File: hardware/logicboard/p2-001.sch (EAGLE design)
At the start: 29 parts, among them IC1 5V, IC2 74LS07N, IC3 4066N, K1 G5V1, T1 2SC1815, U1 DS18B20

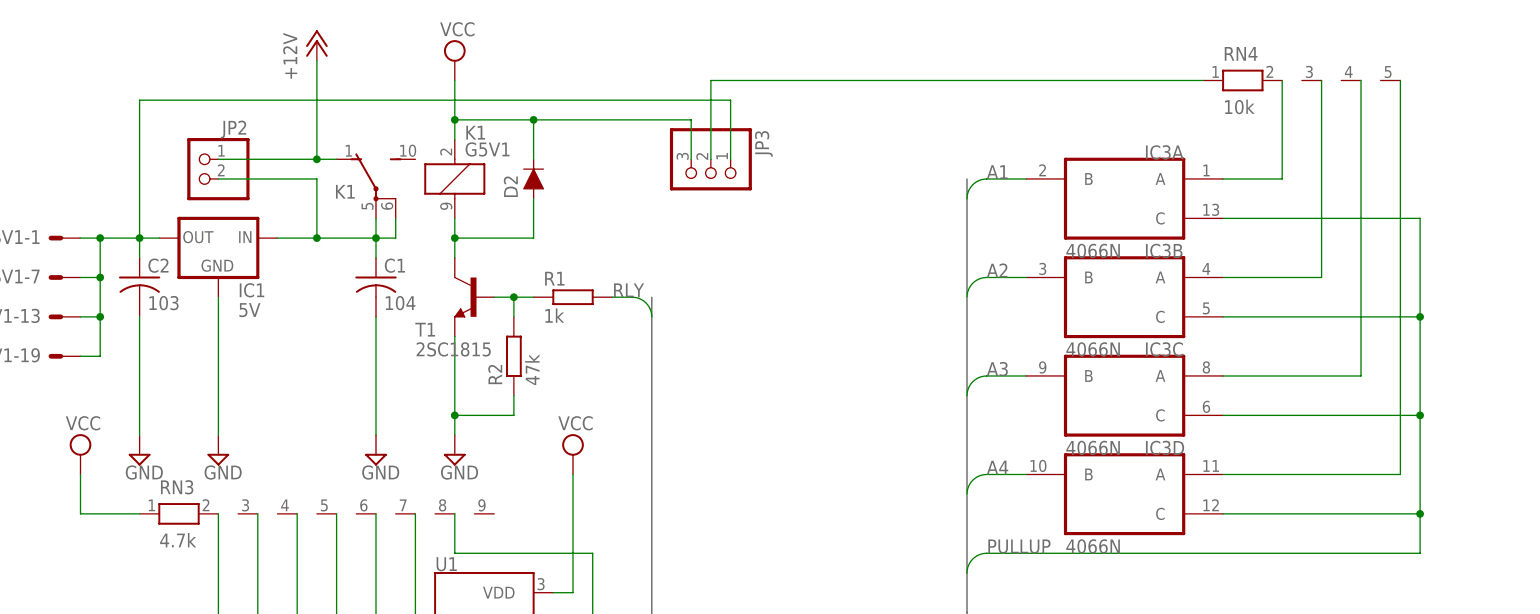
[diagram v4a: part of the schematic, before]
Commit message: Jumper -> SW.
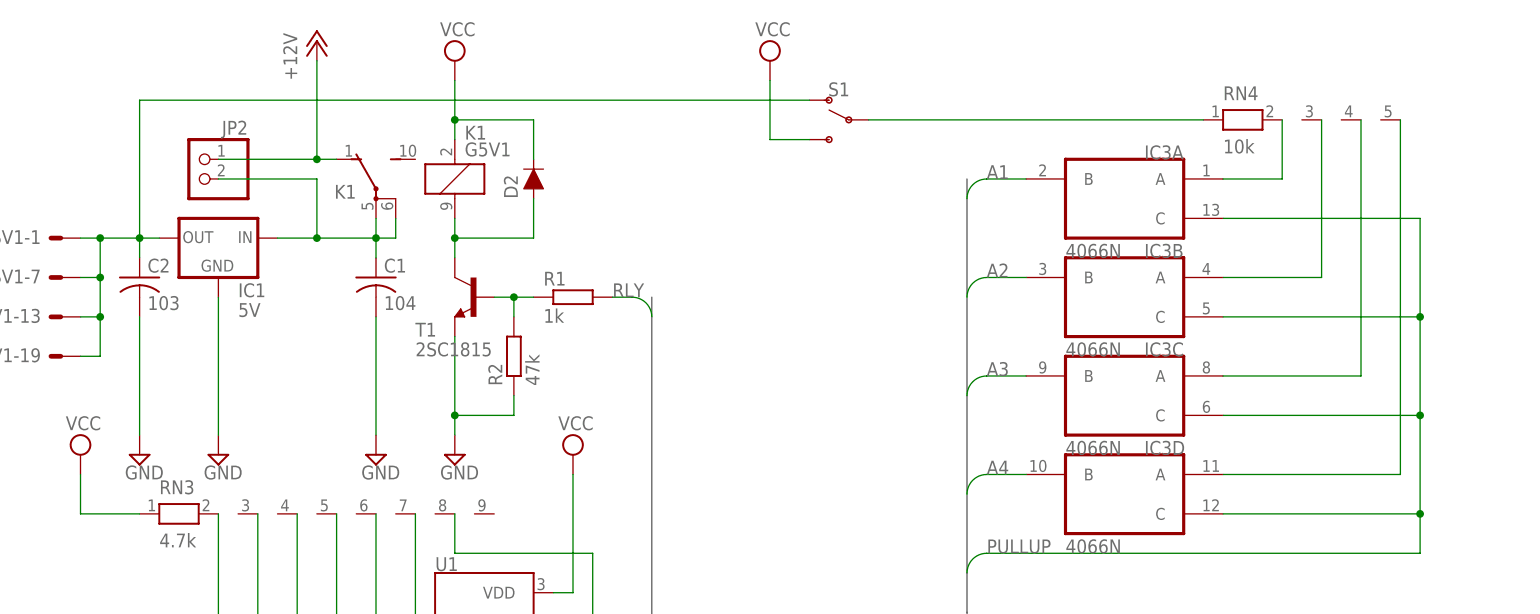
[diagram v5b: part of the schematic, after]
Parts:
- removed JP3: (no value), pinhead:PINHD-1X3
- added S1: (no value), SparkFun-Switches:SWITCH-SPDT-PTH-11.6X4.0MM
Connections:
- removed net N$2: JP3.2, RN4.1
- new net VPULLUP: RN4.1, S1.P
- net VCC: now also S1.S; no longer JP3.3
- net VOUT: now also S1.O; no longer JP3.1
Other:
- moved on the sheet: RN4
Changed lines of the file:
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@@
 <part name="SUPPLY28" library="supply2" deviceset="GND" device=""/>
 <part name="JP2" library="pinhead" library_urn="urn:adsk.eagle:library:325" deviceset="PINHD-1X2" device="" package3d_urn="urn:adsk.eagle:package:22435/2"/>
-<part name="JP3" library="pinhead" library_urn="urn:adsk.eagle:library:325" deviceset="PINHD-1X3" device="" package3d_urn="urn:adsk.eagle:package:22458/2"/>
+<part name="SUPPLY5" library="supply2" library_urn="urn:adsk.eagle:library:372" deviceset="VCC" device=""/>
+<part name="S1" library="SparkFun-Switches" deviceset="SWITCH-SPDT" device="-PTH-11.6X4.0MM"/>
 </parts>
 <sheets>
@@
 <attribute name="VALUE" x="122.555" y="6.985" size="1.778" layer="96"/>
 </instance>
-<instance part="RN4" gate="1" x="175.26" y="248.92" smashed="yes">
-<attribute name="NAME" x="172.72" y="251.46" size="1.778" layer="95"/>
-<attribute name="VALUE" x="172.72" y="244.602" size="1.778" layer="96"/>
+<instance part="RN4" gate="1" x="175.26" y="243.84" smashed="yes">
+<attribute name="NAME" x="172.72" y="246.38" size="1.778" layer="95"/>
+<attribute name="VALUE" x="172.72" y="239.522" size="1.778" layer="96"/>
 </instance>
 <instance part="IC3" gate="A" x="160.02" y="233.68" smashed="yes" rot="MR0">
@@
 <attribute name="VALUE" x="46.99" y="231.14" size="1.778" layer="96" rot="MR0"/>
 </instance>
-<instance part="JP3" gate="A" x="106.68" y="236.22" smashed="yes" rot="R270">
-<attribute name="NAME" x="112.395" y="242.57" size="1.778" layer="95" rot="R270"/>
-<attribute name="VALUE" x="99.06" y="242.57" size="1.778" layer="96" rot="R270"/>
+<instance part="SUPPLY5" gate="G$1" x="114.3" y="251.46" smashed="yes">
+<attribute name="VALUE" x="112.395" y="254.635" size="1.778" layer="96"/>
+</instance>
+<instance part="S1" gate="1" x="124.46" y="243.84" smashed="yes" rot="MR0">
+<attribute name="NAME" x="123.19" y="246.888" size="1.778" layer="95" font="vector" rot="MR0" align="bottom-center"/>
+<attribute name="VALUE" x="123.444" y="240.538" size="1.778" layer="96" font="vector" rot="MR0" align="top-center"/>
 </instance>
 </instances>
@@
 <wire x1="83.82" y1="243.84" x2="73.66" y2="243.84" width="0.1524" layer="91"/>
 <junction x="73.66" y="243.84"/>
-<pinref part="JP3" gate="A" pin="3"/>
-<wire x1="83.82" y1="243.84" x2="104.14" y2="243.84" width="0.1524" layer="91"/>
-<wire x1="104.14" y1="243.84" x2="104.14" y2="238.76" width="0.1524" layer="91"/>
-<junction x="83.82" y="243.84"/>
 </segment>
 <segment>
@@
 <pinref part="U1" gate="G$1" pin="VDD"/>
 <wire x1="88.9" y1="182.88" x2="86.36" y2="182.88" width="0.1524" layer="91"/>
+</segment>
+<segment>
+<pinref part="SUPPLY5" gate="G$1" pin="VCC"/>
+<wire x1="114.3" y1="248.92" x2="114.3" y2="241.3" width="0.1524" layer="91"/>
+<pinref part="S1" gate="1" pin="S"/>
+<wire x1="114.3" y1="241.3" x2="119.38" y2="241.3" width="0.1524" layer="91"/>
 </segment>
 </net>
@@
 <wire x1="27.94" y1="213.36" x2="27.94" y2="218.44" width="0.1524" layer="91"/>
 <junction x="27.94" y="218.44"/>
-<pinref part="JP3" gate="A" pin="1"/>
 <wire x1="33.02" y1="246.38" x2="33.02" y2="228.6" width="0.1524" layer="91"/>
-<wire x1="109.22" y1="238.76" x2="109.22" y2="246.38" width="0.1524" layer="91"/>
-<wire x1="109.22" y1="246.38" x2="33.02" y2="246.38" width="0.1524" layer="91"/>
+<wire x1="119.38" y1="246.38" x2="33.02" y2="246.38" width="0.1524" layer="91"/>
+<pinref part="S1" gate="1" pin="O"/>
 </segment>
 </net>
@@
 <segment>
 <pinref part="RN4" gate="1" pin="2"/>
-<wire x1="180.34" y1="248.92" x2="180.34" y2="236.22" width="0.1524" layer="91"/>
+<wire x1="180.34" y1="243.84" x2="180.34" y2="236.22" width="0.1524" layer="91"/>
 <pinref part="IC3" gate="A" pin="A"/>
 <wire x1="180.34" y1="236.22" x2="172.72" y2="236.22" width="0.1524" layer="91"/>
@@
 <segment>
 <pinref part="RN4" gate="1" pin="3"/>
-<wire x1="185.42" y1="248.92" x2="185.42" y2="223.52" width="0.1524" layer="91"/>
+<wire x1="185.42" y1="243.84" x2="185.42" y2="223.52" width="0.1524" layer="91"/>
 <pinref part="IC3" gate="B" pin="A"/>
 <wire x1="185.42" y1="223.52" x2="172.72" y2="223.52" width="0.1524" layer="91"/>
@@
 <pinref part="RN4" gate="1" pin="4"/>
 <pinref part="IC3" gate="C" pin="A"/>
-<wire x1="190.5" y1="248.92" x2="190.5" y2="210.82" width="0.1524" layer="91"/>
+<wire x1="190.5" y1="243.84" x2="190.5" y2="210.82" width="0.1524" layer="91"/>
 <wire x1="190.5" y1="210.82" x2="172.72" y2="210.82" width="0.1524" layer="91"/>
 </segment>
@@
 <pinref part="RN4" gate="1" pin="5"/>
 <pinref part="IC3" gate="D" pin="A"/>
-<wire x1="195.58" y1="248.92" x2="195.58" y2="198.12" width="0.1524" layer="91"/>
+<wire x1="195.58" y1="243.84" x2="195.58" y2="198.12" width="0.1524" layer="91"/>
 <wire x1="195.58" y1="198.12" x2="172.72" y2="198.12" width="0.1524" layer="91"/>
 </segment>
@@
 </segment>
 </net>
-<net name="N$2" class="0">
+<net name="VPULLUP" class="0">
 <segment>
 <pinref part="RN4" gate="1" pin="1"/>
-<wire x1="170.18" y1="248.92" x2="106.68" y2="248.92" width="0.1524" layer="91"/>
-<pinref part="JP3" gate="A" pin="2"/>
-<wire x1="106.68" y1="248.92" x2="106.68" y2="238.76" width="0.1524" layer="91"/>
-</segment>
-</net>
+<wire x1="127" y1="243.84" x2="170.18" y2="243.84" width="0.1524" layer="91"/>
+<pinref part="S1" gate="1" pin="P"/>
+</segment>
+</net>

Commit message: Replaced back-panel SW to LEDSW. Now Back port is incompatible to 2.0.0-X.
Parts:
- added R3: 1k, resistor:R-EU_0204/5
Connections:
- net N$1 renamed V+12V
- removed net VDD: MC1.3V, SV2-19.S
- new net PWRLED: R3.1, SV2-5.S
- net +12V: now also R3.2
- net GND: now also SV2-10.S, SV2-6.S; no longer SV2-20.S, SV2-8.S
- net MINRTN: now also SV2-8.S; no longer SV2-6.S
- net MINSND: now also SV2-7.S; no longer SV2-5.S
- net MO1RTN: now also SV2-13.S; no longer SV2-11.S
- net MO1SND: now also SV2-12.S; no longer SV2-10.S
- net MO2RTN: now also SV2-18.S; no longer SV2-16.S
- net MO2SND: now also SV2-17.S; no longer SV2-15.S
- net MTHRTN: now also SV2-20.S; no longer SV2-18.S
- net MTHSND: now also SV2-19.S; no longer SV2-17.S
- net THS: now also SV2-11.S; no longer SV2-9.S
- net VCC: now also SV2-9.S; no longer SV2-7.S
- net XLEDB: now also SV2-15.S; no longer SV2-13.S
- net XLEDG: now also SV2-14.S; no longer SV2-12.S
- net XLEDR: now also SV2-16.S; no longer SV2-14.S
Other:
- moved on the sheet: SV2-10, SV2-11, SV2-12, SV2-13, SV2-14, SV2-15, SV2-16, SV2-17, SV2-18, SV2-19, SV2-2, SV2-20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

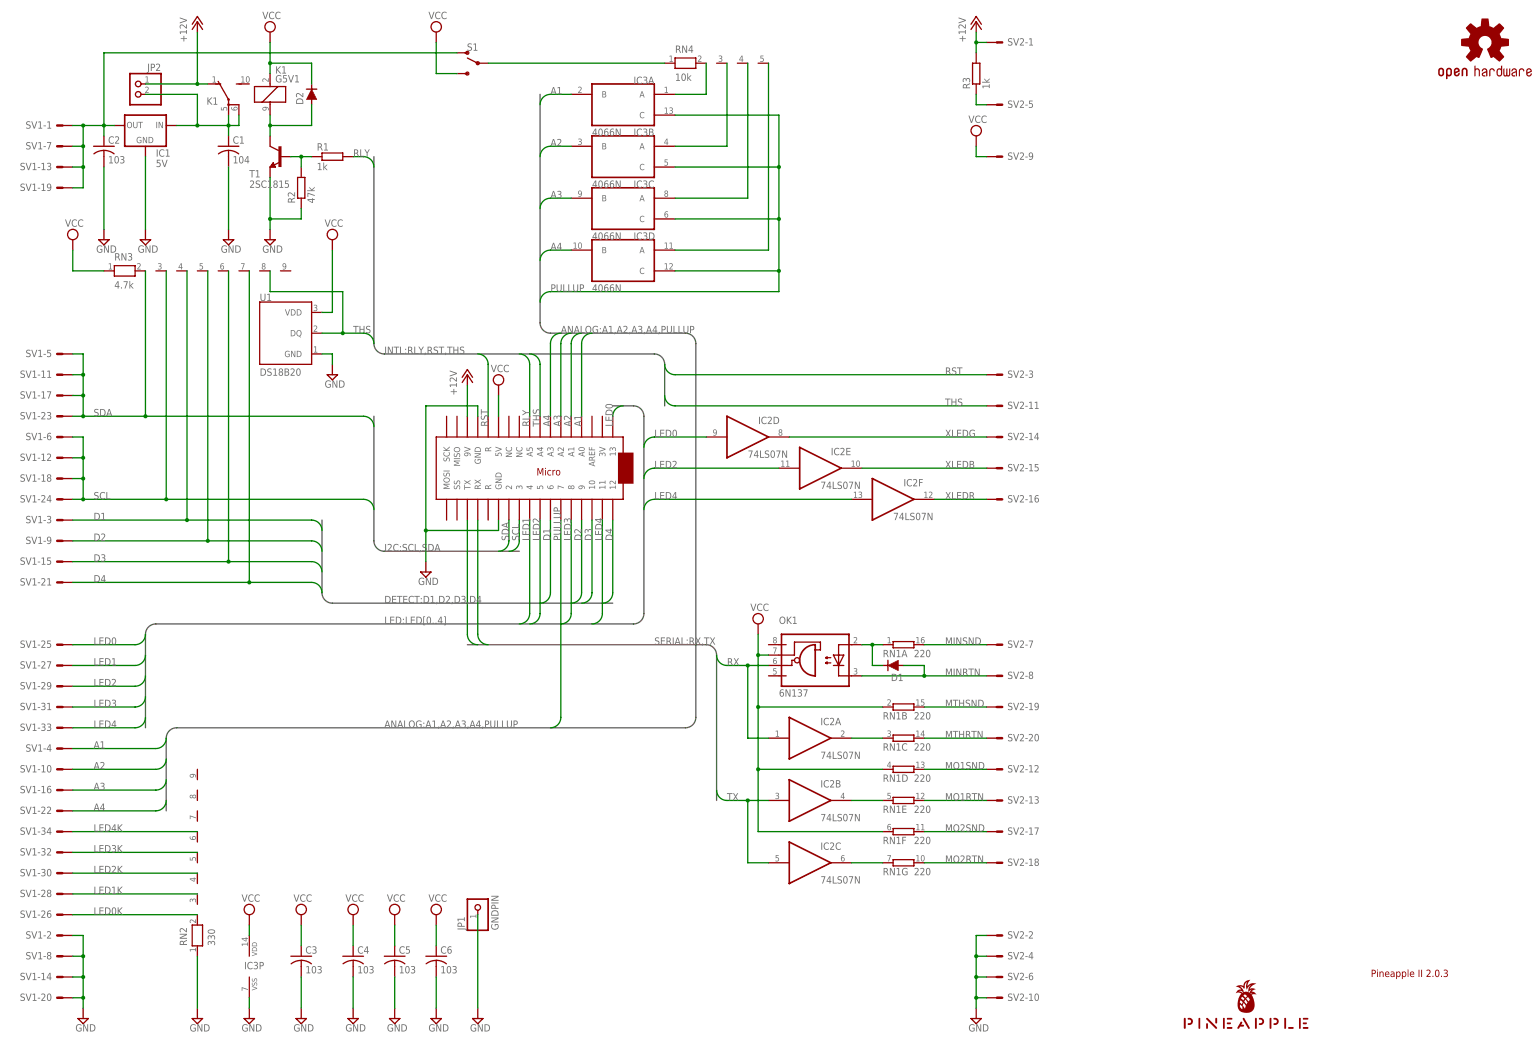
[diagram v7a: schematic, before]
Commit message: Added RS-422 TX driver.
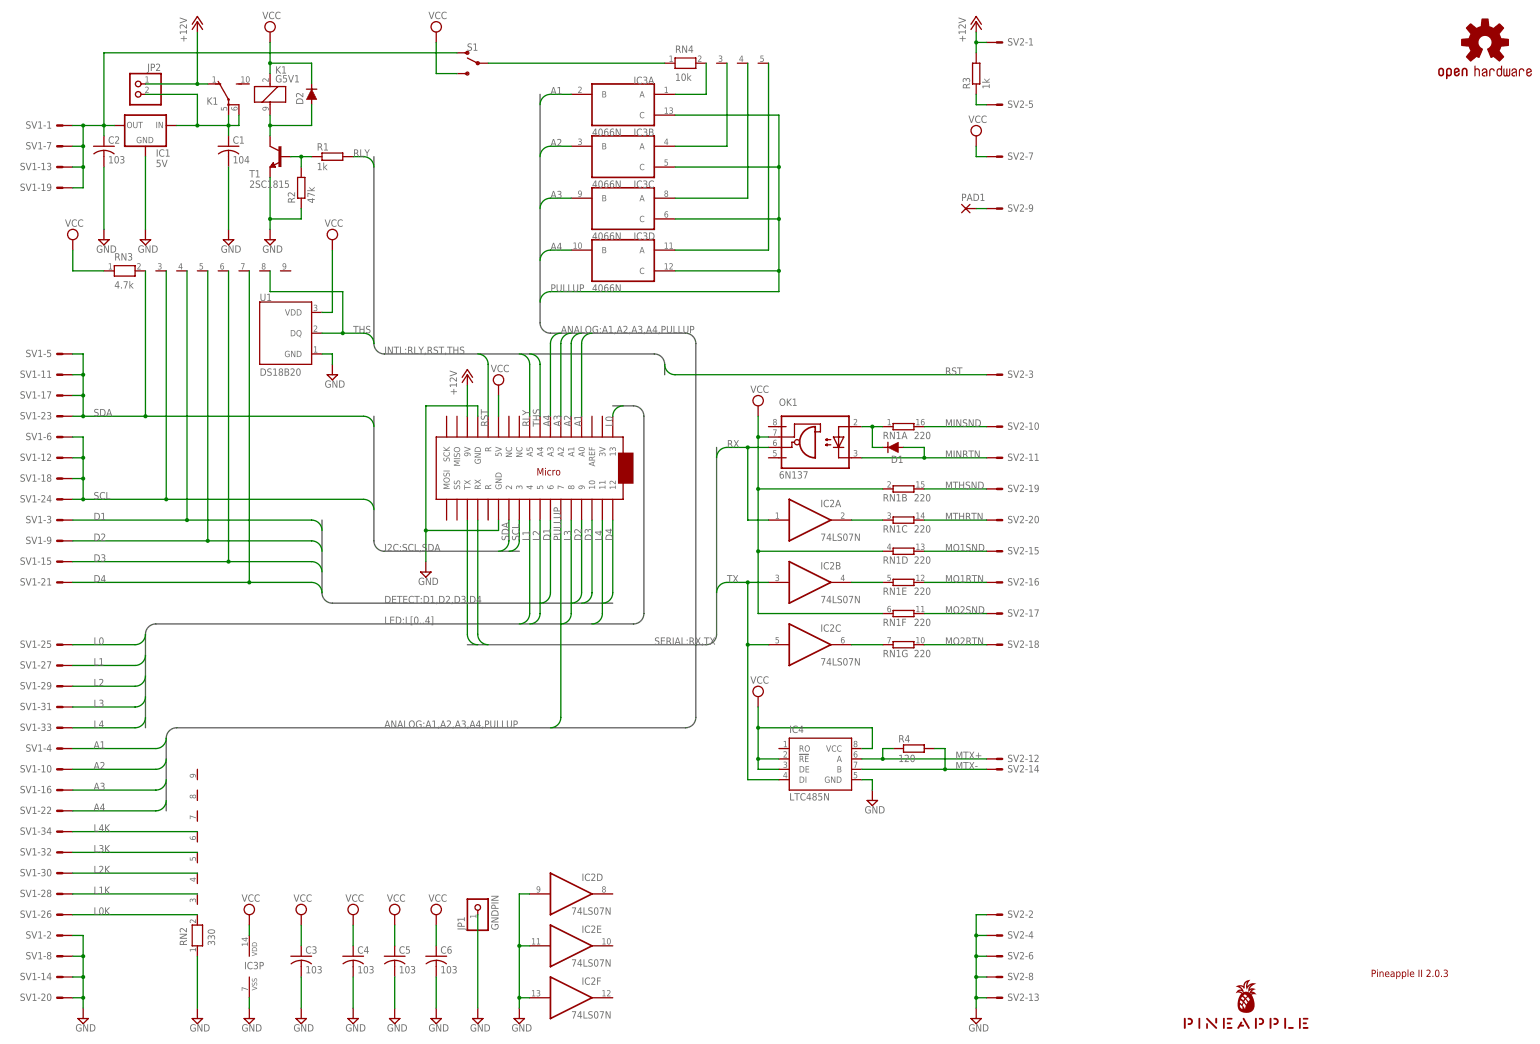
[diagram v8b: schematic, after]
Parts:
- added IC4: LTC485N, linear-technology:LTC485N
- added PAD1: (no value), wirepad:1,6/0,8
- added R4: 120, resistor:R-EU_0204/5
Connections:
- net LED0K renamed L0K
- net LED1 renamed L1
- net LED1K renamed L1K
- net LED2K renamed L2K
- net LED3 renamed L3
- net LED3K renamed L3K
- net LED4K renamed L4K
- removed net LED0: IC2D.I, MC1.13, SV1-25.S
- removed net LED2: IC2E.I, MC1.5, SV1-29.S
- removed net LED4: IC2F.I, MC1.11, SV1-33.S
- removed net XLEDB: IC2E.O, SV2-15.S
- removed net XLEDG: IC2D.O, SV2-14.S
- removed net XLEDR: IC2F.O, SV2-16.S
- new net L0: MC1.13, SV1-25.S
- new net L2: MC1.5, SV1-29.S
- new net L4: MC1.11, SV1-33.S
- new net MTX+: IC4.A, R4.1, SV2-12.S
- new net MTX-: IC4.B, R4.2, SV2-14.S
- new net N$1: PAD1.P, SV2-9.S
- net GND: now also IC2D.I, IC2E.I, IC2F.I, IC4.GND, SV2-13.S, SV2-8.S; no longer SV2-10.S
- net MINRTN: now also SV2-11.S; no longer SV2-8.S
- net MINSND: now also SV2-10.S; no longer SV2-7.S
- net MO1RTN: now also SV2-16.S; no longer SV2-13.S
- net MO1SND: now also SV2-15.S; no longer SV2-12.S
- net THS: no longer SV2-11.S
- net TX: now also IC4.DI
- net VCC: now also IC4.!RE, IC4.DE, IC4.VCC, SV2-7.S; no longer SV2-9.S
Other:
- moved on the sheet: D1, IC2A, IC2B, IC2C, IC2D, IC2E, IC2F, OK1, RN1A, RN1B, RN1C, RN1D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
